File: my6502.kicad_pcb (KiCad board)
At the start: 2 copper layers, 170 x 150 mm, 49 parts, among them U1 74HC00, U10 74HC00, U11 74HC00, U12 74HC00, U13 74HC00, U14 74HC00, U15 74HC00, U16 74HC00, U17 74HC00, U18 LM555xN, U2 LM555xN, U3 W65C02S, U4 LM555xN, U5 28C256, U6 65C22, U7 CY62256-70PC, U9 74HC00, X1 CXO_DIP14

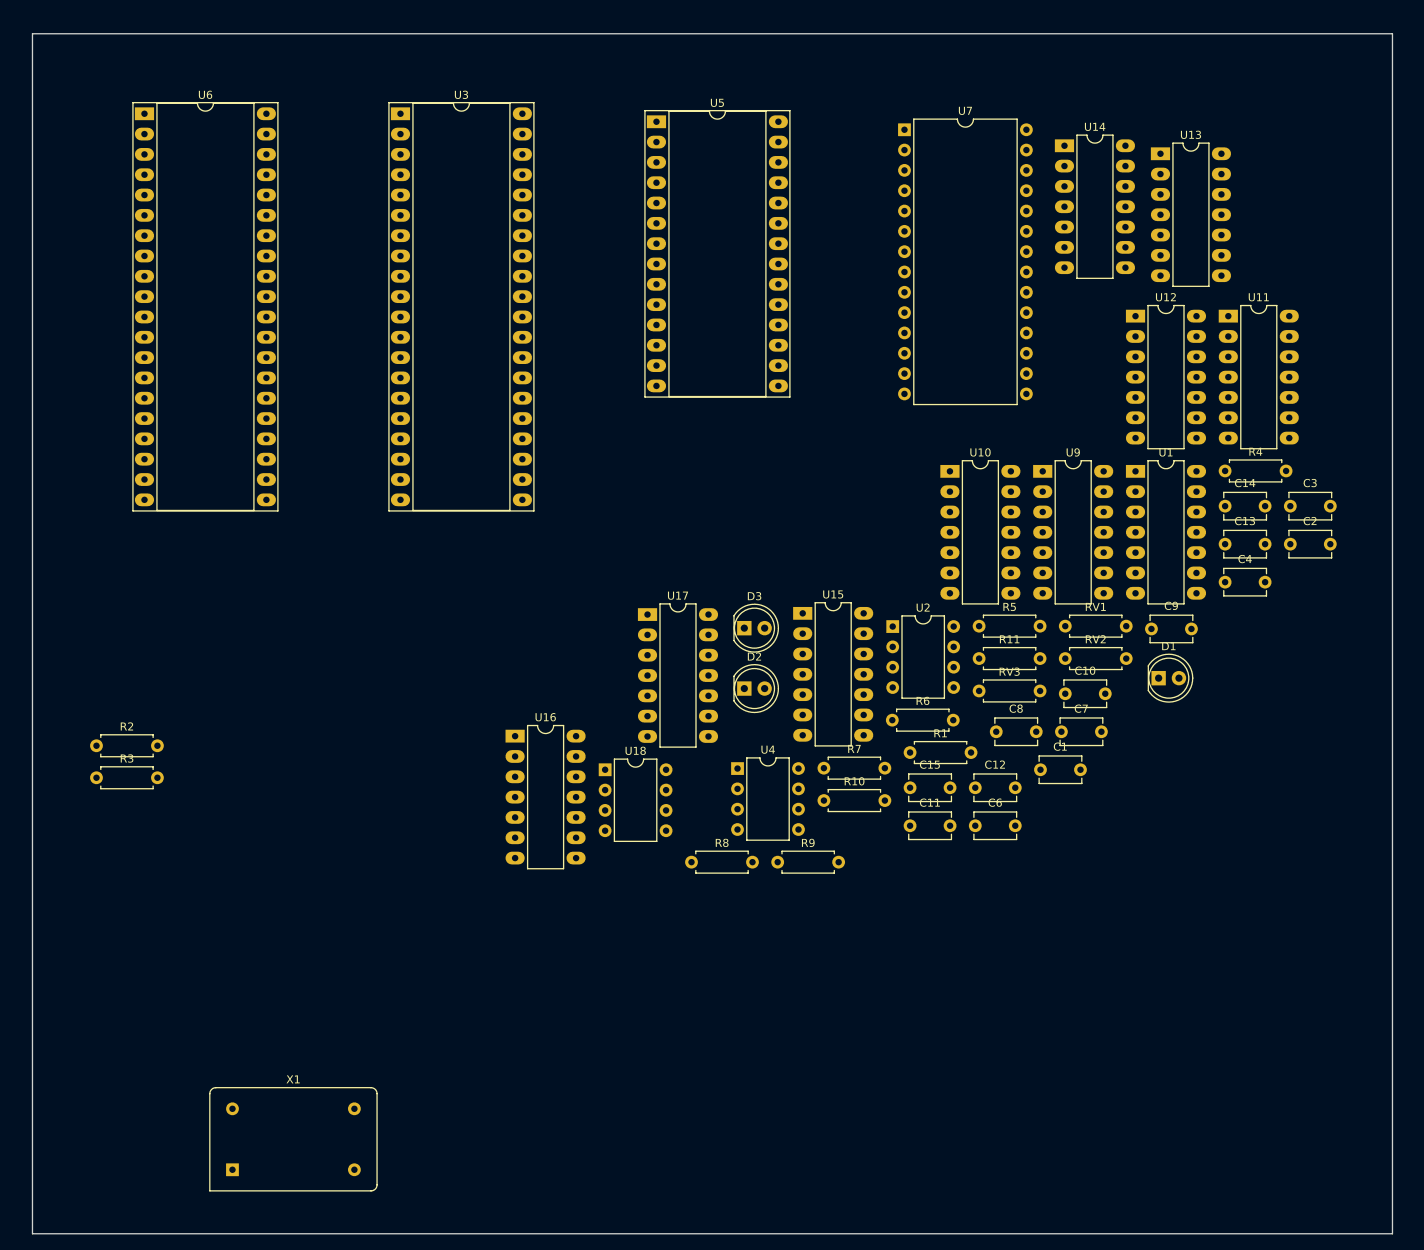
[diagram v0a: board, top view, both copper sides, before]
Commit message: placed most components
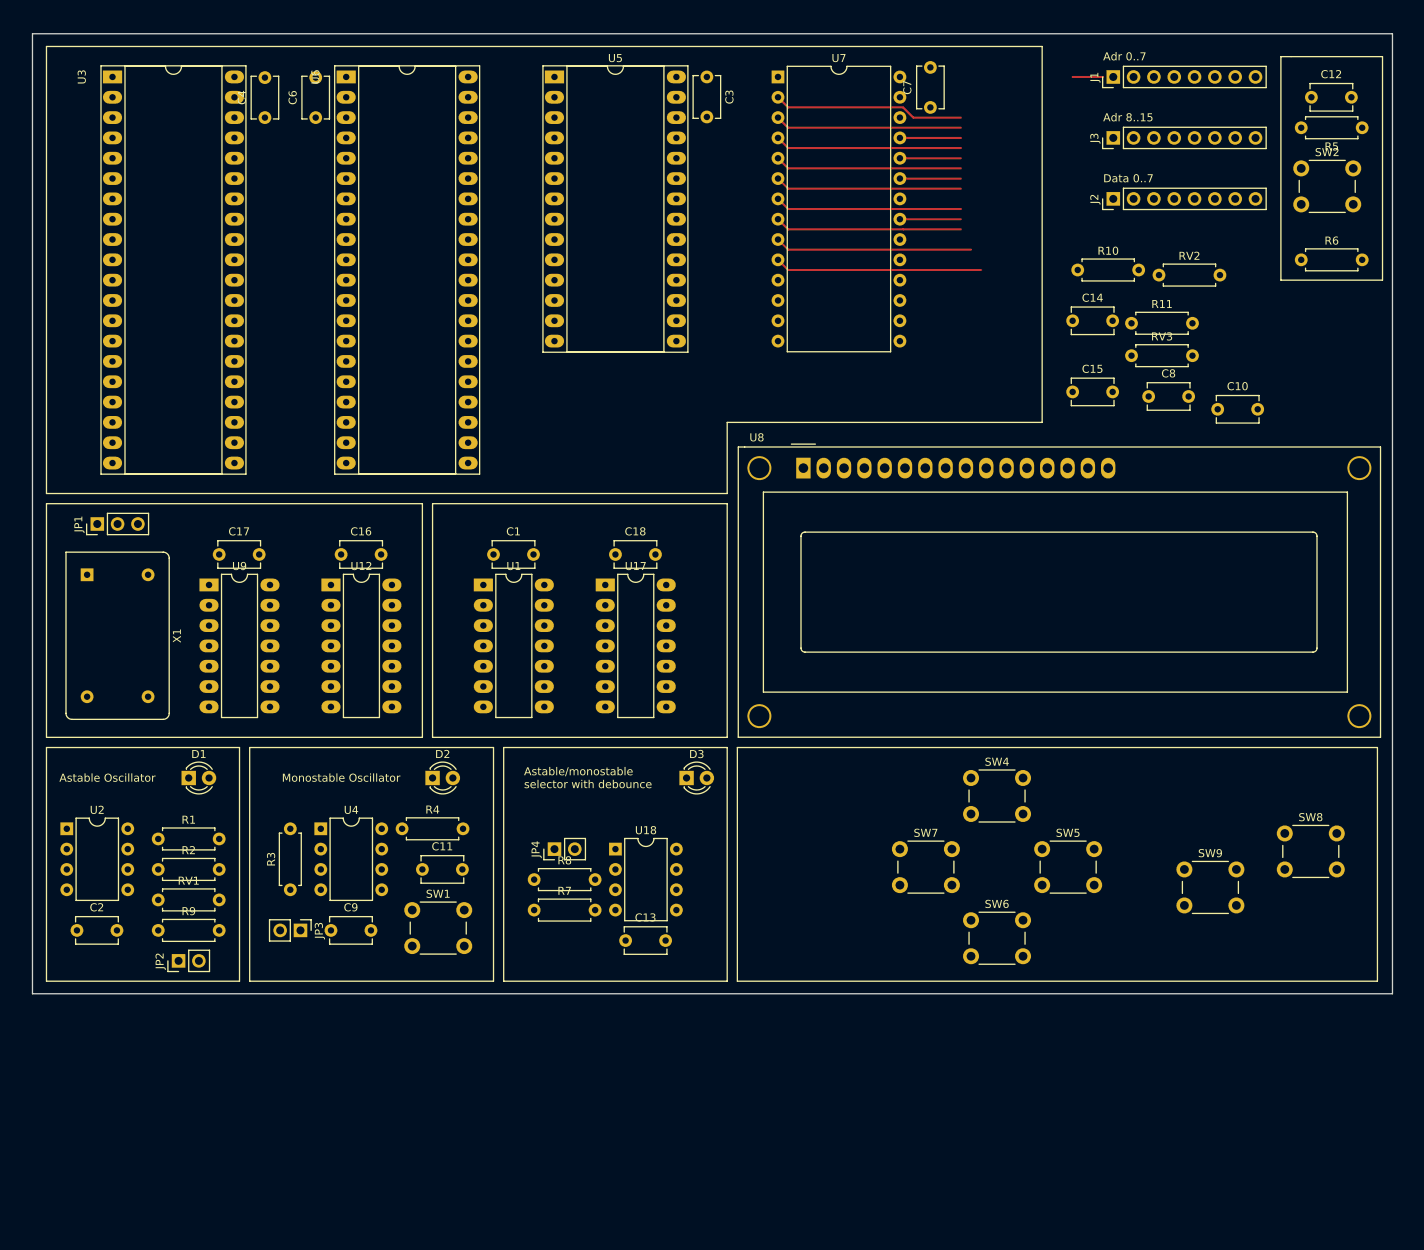
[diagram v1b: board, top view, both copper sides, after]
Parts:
- removed U10, U11, U13, U14, U15, U16: 74HC00, Package_DIP:DIP-14_W7.62mm_LongPads
- added C16: 100n, Capacitor_THT:C_Disc_D5.1mm_W3.2mm_P5.00mm, F.Cu at (68.6, 85.1)
- added C17: 100n, Capacitor_THT:C_Disc_D5.1mm_W3.2mm_P5.00mm, F.Cu at (53.3, 85.1)
- added C18: 100n, Capacitor_THT:C_Disc_D5.1mm_W3.2mm_P5.00mm, F.Cu at (102.9, 85.1)
- added J1: Conn_01x08, Connector_PinHeader_2.54mm:PinHeader_1x08_P2.54mm_Vertical, F.Cu at (165.1, 25.4)
- added J2: Conn_01x08, Connector_PinHeader_2.54mm:PinHeader_1x08_P2.54mm_Vertical, F.Cu at (165.1, 40.6)
- added J3: Conn_01x08, Connector_PinHeader_2.54mm:PinHeader_1x08_P2.54mm_Vertical, F.Cu at (165.1, 33.0)
- added JP1: Jumper_3_Open, Connector_PinHeader_2.54mm:PinHeader_1x03_P2.54mm_Vertical, F.Cu at (38.1, 81.3)
- added JP2: Jumper_2_Open, Connector_PinHeader_2.54mm:PinHeader_1x02_P2.54mm_Vertical, F.Cu at (48.3, 135.9)
- added JP3: Jumper_2_Open, Connector_PinHeader_2.54mm:PinHeader_1x02_P2.54mm_Vertical, F.Cu at (63.5, 132.1)
- added JP4: Jumper_2_Open, Connector_PinHeader_2.54mm:PinHeader_1x02_P2.54mm_Vertical, F.Cu at (95.2, 121.9)
- added SW1: Switch, Button_Switch_THT:SW_PUSH_6mm, F.Cu at (77.5, 129.5)
- added SW2: SW_MEC_5G, Button_Switch_THT:SW_PUSH_6mm, F.Cu at (188.6, 36.8)
- added SW4: SW_Push, Button_Switch_THT:SW_PUSH_6mm, F.Cu at (147.3, 113.0)
- added SW5: SW_Push, Button_Switch_THT:SW_PUSH_6mm, F.Cu at (156.2, 121.9)
- added SW6: SW_Push, Button_Switch_THT:SW_PUSH_6mm, F.Cu at (147.3, 130.8)
- added SW7: SW_Push, Button_Switch_THT:SW_PUSH_6mm, F.Cu at (138.4, 121.9)
- added SW8: SW_Push, Button_Switch_THT:SW_PUSH_6mm, F.Cu at (186.5, 120.0)
- added SW9: SW_Push, Button_Switch_THT:SW_PUSH_6mm, F.Cu at (174.0, 124.5)
- added U8: HD44780, Display:WC1602A, F.Cu at (126.4, 74.3)
- D1, D2, D3: footprint LED_THT:LED_D5.0mm -> LED_THT:LED_D3.0mm
- moved C2 159.2 mm to (35.6, 132.1)
- moved C4 133.3 mm to (59.1, 30.5), turned to 90 degrees
- moved D1 121.9 mm to (49.5, 113.0)
- moved C6 121.0 mm to (65.4, 30.5), turned to 90 degrees
- moved RV1 118.4 mm to (45.7, 128.3)
- moved R4 112.2 mm to (76.2, 119.4)
- moved C9 109.3 mm to (67.3, 132.1)
- moved U2 106.3 mm to (34.3, 119.4)
- moved U12 106.0 mm to (67.3, 88.9)
- moved U9 105.2 mm to (52.1, 88.9)
- moved C12 96.0 mm to (189.9, 27.9)
- moved R1 94.6 mm to (45.7, 120.7)
- moved C3 90.5 mm to (114.3, 25.4), turned to 270 degrees
- moved C13 89.8 mm to (104.1, 133.3)
- moved U1 82.7 mm to (86.4, 88.9)
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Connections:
- R10 pad 2: (no net) -> Net-(JP3-Pad2)
- R11 pad 2: (no net) -> Net-(JP4-Pad2)
- R9 pad 2: (no net) -> Net-(JP2-Pad2)
- RV2 pad 2: (no net) -> Net-(RV2-Pad2)
- RV3 pad 2: (no net) -> Net-(RV3-Pad2)
- U1 pad 1: Net-(U1-Pad1) -> /A15
- U1 pad 11: /~A15 -> Net-(U1-Pad11)
- U1 pad 12: /A15 -> Net-(U1-Pad12)
- U1 pad 13: /A15 -> /A12
- U1 pad 2: /A12 -> /A15
- U1 pad 3: Net-(U1-Pad3) -> /~A15
- U1 pad 8: Net-(U1-Pad1) -> Net-(U1-Pad12)
- U12 pad 10: (no net) -> Net-(U12-Pad10)
- U12 pad 12: (no net) -> GND
- U12 pad 13: (no net) -> GND
- U12 pad 14: (no net) -> +5V
- U12 pad 4: (no net) -> Net-(JP1-Pad2)
- U12 pad 5: (no net) -> Net-(U12-Pad3)
- U12 pad 6: (no net) -> Net-(U12-Pad10)
- U12 pad 7: (no net) -> GND
- U12 pad 8: (no net) -> CLK
- U12 pad 9: (no net) -> Net-(U12-Pad10)
- U17 pad 10: (no net) -> GND
- U17 pad 12: (no net) -> GND
- U17 pad 13: (no net) -> GND
- U17 pad 2: Net-(U1-Pad3) -> Net-(U1-Pad11)
- U17 pad 4: (no net) -> GND
- U17 pad 5: (no net) -> GND
- U17 pad 9: (no net) -> GND
- U6 pad 10: (no net) -> /PB0
- U6 pad 11: (no net) -> /PB1
- U6 pad 12: (no net) -> /PB2
- U6 pad 13: (no net) -> /PB3
- U6 pad 14: (no net) -> /PB4
- U6 pad 15: (no net) -> /PB5
- U6 pad 16: (no net) -> /PB6
- U6 pad 17: (no net) -> /PB7
- U6 pad 2: (no net) -> /PA0
- U6 pad 23: Net-(U1-Pad3) -> Net-(U1-Pad11)
- U6 pad 3: (no net) -> /PA1
- U6 pad 4: (no net) -> /PA2
- U6 pad 5: (no net) -> /PA3
- U6 pad 6: (no net) -> /PA4
- U6 pad 7: (no net) -> /PA5
- U6 pad 8: (no net) -> /PA6
- U6 pad 9: (no net) -> /PA7
- U9 pad 10: (no net) -> /MCLK
- U9 pad 11: (no net) -> Net-(JP1-Pad1)
- U9 pad 12: (no net) -> Net-(U9-Pad12)
- U9 pad 13: (no net) -> Net-(U9-Pad13)
- U9 pad 14: (no net) -> +5V
- U9 pad 3: Net-(U13-Pad1) -> Net-(U9-Pad12)
- U9 pad 4: (no net) -> /CLKSEL
- U9 pad 5: (no net) -> /CLKSEL
- U9 pad 6: (no net) -> Net-(U9-Pad6)
- U9 pad 7: (no net) -> GND
- U9 pad 8: (no net) -> Net-(U9-Pad13)
- U9 pad 9: (no net) -> Net-(U9-Pad6)
- X1 pad 8: (no net) -> Net-(JP1-Pad3)
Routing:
- net /A0: track 0.00 -> 29.7 mm
- net /A1: track 0.00 -> 24.7 mm
- net /A12: track 0.00 -> 23.9 mm
- net /A2: track 0.00 -> 23.4 mm
- net /A7: track 0.00 -> 23.4 mm
- net /A6: track 0.00 -> 23.4 mm
- net /A5: track 0.00 -> 23.4 mm
- net /A4: track 0.00 -> 23.4 mm
- net /A3: track 0.00 -> 23.4 mm
- net /A9: track 0.00 -> 7.62 mm
- net /A8: track 0.00 -> 7.62 mm
- net /A11: track 0.00 -> 7.62 mm
- net /A10: track 0.00 -> 7.62 mm
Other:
- board size 170 x 150 mm -> 170 x 120 mm
- board text added: "Adr 0..7"
- board text added: "Adr 8..15"
- board text added: "Astable Oscillator"
- board text added: "Astable/monostable selector with debounce"
- board text added: "Data 0..7"
- board text added: "IKEA Västanhed has inner passpartout size 17x12 cm."
- board text added: "Monostable Oscillator"

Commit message: USB connector, overvoltage protection, ...
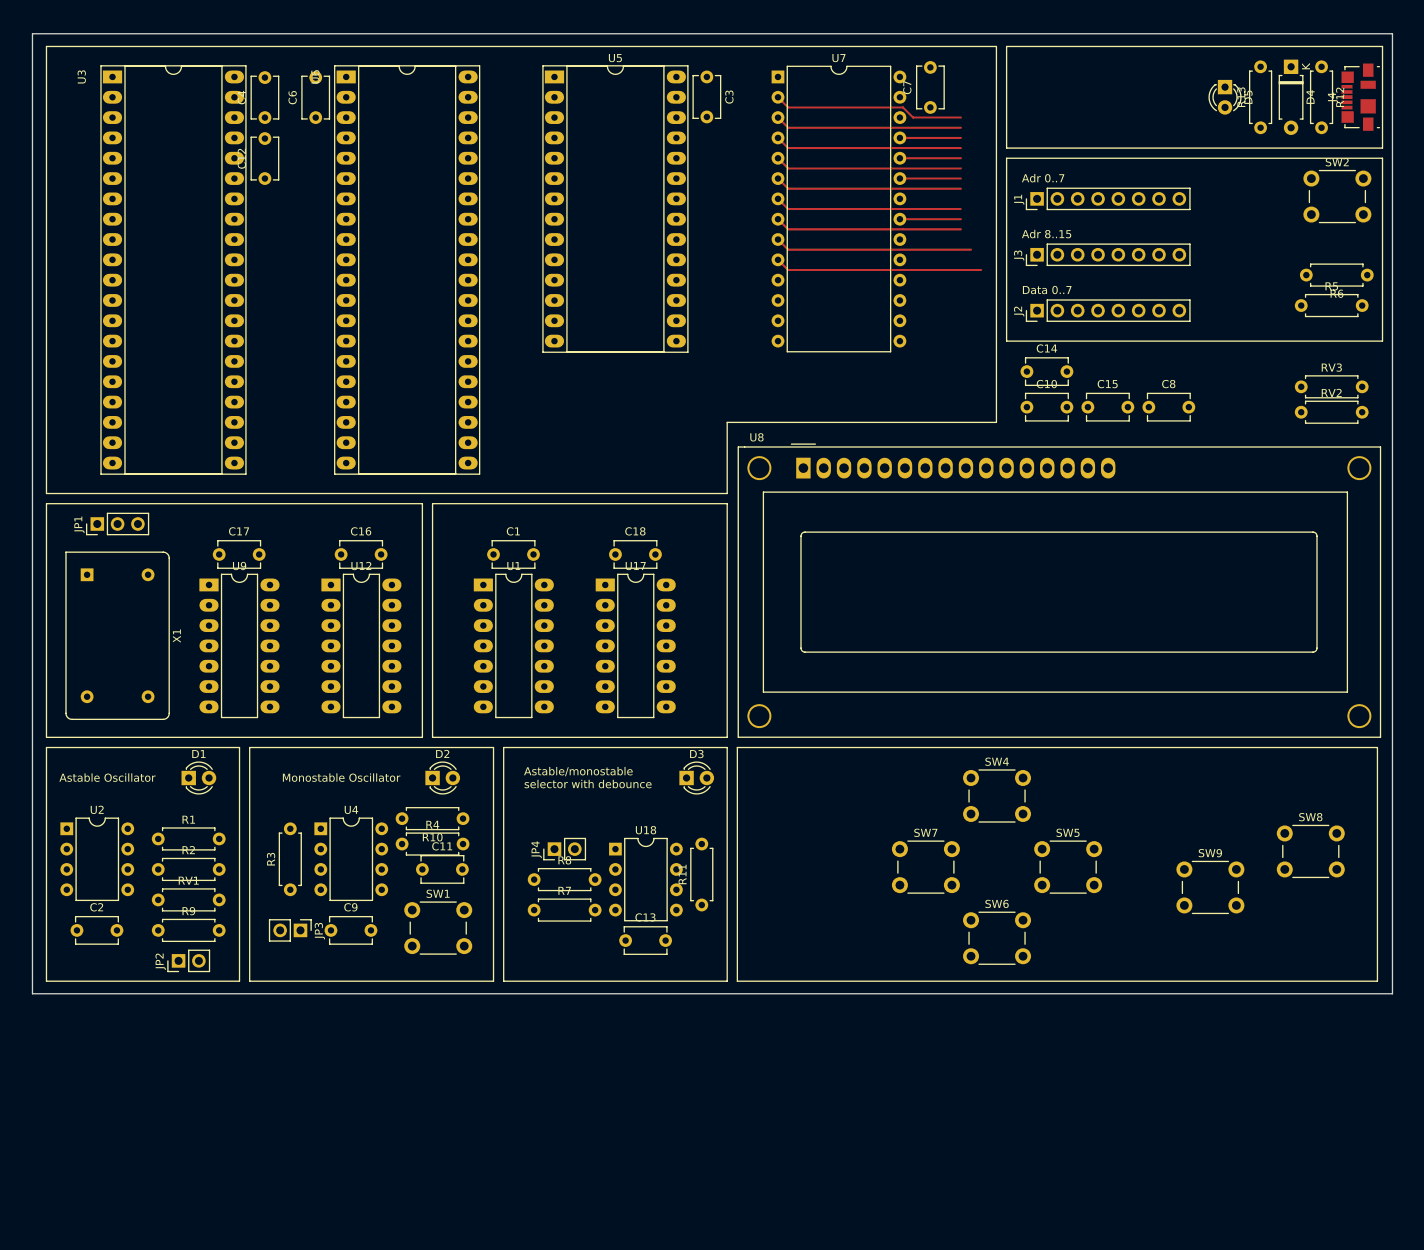
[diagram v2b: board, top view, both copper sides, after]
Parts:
- added D4: D_Zener, Diode_THT:D_A-405_P7.62mm_Horizontal, F.Cu at (187.3, 24.1)
- added D5: LED, LED_THT:LED_D3.0mm, F.Cu at (179.1, 26.7)
- added J4: USB_B_Micro, Connector_USB:USB_Micro-B_Molex_47346-0001, F.Cu at (195.8, 27.9)
- added R12: ? (low res), Resistor_THT:R_Axial_DIN0207_L6.3mm_D2.5mm_P7.62mm_Horizontal, F.Cu at (191.1, 24.1)
- added R13: 220, Resistor_THT:R_Axial_DIN0207_L6.3mm_D2.5mm_P7.62mm_Horizontal, F.Cu at (183.5, 31.8)
- moved C12 131.2 mm to (59.1, 38.1), turned to 90 degrees
- moved R10 103.0 mm to (83.8, 118.1), turned to 180 degrees
- moved R11 90.4 mm to (113.7, 128.9), turned to 90 degrees
- moved RV2 24.7 mm to (188.6, 67.3)
- moved C10 23.8 mm to (154.3, 66.7)
- moved R5 23.5 mm to (188.6, 54.0), turned to 0 degrees
- moved RV3 21.6 mm to (188.6, 64.1)
- moved J1 18.0 mm to (155.6, 40.6)
- moved J3 17.4 mm to (155.6, 47.6)
- moved J2 16.9 mm to (155.6, 54.6)
- moved C14 8.54 mm to (154.3, 62.2)
- moved R6 8.47 mm to (196.8, 50.2), turned to 180 degrees
- moved C15 2.69 mm to (161.9, 66.7)
- moved R4 1.91 mm to (76.2, 121.3)
- moved SW2 1.80 mm to (189.9, 38.1)
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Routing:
- net /A0: track 29.7 -> 25.9 mm

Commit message: Mostly minor adjustments
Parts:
- RV2, RV3: footprint Resistor_THT:R_Axial_DIN0207_L6.3mm_D2.5mm_P7.62mm_Horizontal -> Potentiometer_THT:Potentiometer_Piher_PT-6-V_Vertical
- moved J4 157.1 mm to (38.7, 23.9), turned to 180 degrees
- moved R12 156.3 mm to (34.9, 28.6), turned to 0 degrees
- moved R6 155.6 mm to (42.5, 70.5)
- moved SW2 155.6 mm to (35.6, 58.4)
- moved R5 155.0 mm to (34.9, 74.3)
- moved D4 152.6 mm to (34.9, 32.4), turned to 0 degrees
- moved D5 142.4 mm to (37.5, 41.9), turned to 0 degrees
- moved R13 141.0 mm to (42.5, 36.2), turned to 180 degrees
- moved C14 125.6 mm to (40.6, 115.6), turned to 180 degrees
- moved C10 95.4 mm to (72.4, 115.6), turned to 180 degrees
- moved C15 73.6 mm to (109.2, 118.1), turned to 180 degrees
- moved C8 36.9 mm to (132.7, 68.6), turned to 180 degrees
- moved J1 23.3 mm to (177.2, 31.8)
- moved J2 23.3 mm to (177.2, 45.7)
- moved J3 23.3 mm to (177.2, 38.7)
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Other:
- board text added: "Astable/monostable"
- board text added: "Bus monitor/extension"
- board text added: "CPU"
- board text added: "Display"
- board text added: "EEPROM"
- board text added: "I/O"
- board text added: "Input"
- board text added: "Memory mappers"
- board text added: "Power"
- board text added: "RAM"
- board text added: "Reset"
- board text added: "selector with debounce"
- board text removed: "Astable/monostable selector with debounce"
